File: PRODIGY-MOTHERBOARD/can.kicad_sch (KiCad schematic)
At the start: 1 part, among them U12 SN65HVD232

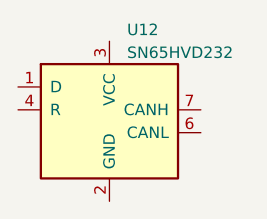
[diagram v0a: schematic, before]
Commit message: project restructure done. Hierarchical sheet done. Outputs/breakouts sheet done
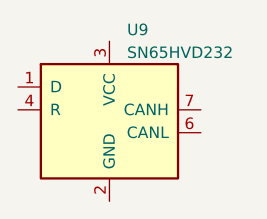
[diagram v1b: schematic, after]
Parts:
- renumbered U12 to U9
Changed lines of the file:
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@@
-(kicad_sch (version 20230121) (generator eeschema)
-  (paper "A4")
-  (symbol (lib_id "Interface_CAN_LIN:SN65HVD232") (at 138.43 93.98 0) (unit 1)
-    (in_bom yes) (on_board yes) (dnp no) (fields_autoplaced)
-    (property "Reference" "U12" (at 140.3859 85.09 0)
-      (effects (font (size 1.27 1.27)) (justify left))
-    )
-    (property "Value" "SN65HVD232" (at 140.3859 87.63 0)
-      (effects (font (size 1.27 1.27)) (justify left))
-    )
-    (property "Footprint" "Package_SO:SOIC-8_3.9x4.9mm_P1.27mm" (at 138.43 106.68 0)
-      (effects (font (size 1.27 1.27)) hide)
-    )
-    (property "Datasheet" "http://www.ti.com/lit/ds/symlink/sn65hvd230.pdf" (at 135.89 83.82 0)
-      (effects (font (size 1.27 1.27)) hide)
-    )
-    (pin "1")
-    (pin "2")
-    (pin "3")
-    (pin "4")
-    (pin "5")
-    (pin "6")
-    (pin "7")
-    (pin "8")
-    (instances
-      (project "PRODIGY-MOTHERBOARD"
-        (path "/f1c25860-8989-4190-bd24-2491d23ca7d9/cf0d8bf1-4632-49df-9398-b3de35528304"
-          (reference "U12") (unit 1)
-        )
-      )
-    )
-  )
+(kicad_sch
+	(version 20231120)
+	(generator "eeschema")
+	(generator_version "8.0")
+	(paper "A4")
+	(symbol
+		(lib_id "Interface_CAN_LIN:SN65HVD232")
+		(at 138.43 93.98 0)
+		(unit 1)
+		(exclude_from_sim no)
+		(in_bom yes)
+		(on_board yes)
+		(dnp no)
+		(fields_autoplaced yes)
+		(property "Reference" "U9"
+			(at 140.3859 85.09 0)
+			(effects
+				(font
+					(size 1.27 1.27)
+				)
+				(justify left)
+			)
+		)
+		(property "Value" "SN65HVD232"
+			(at 140.3859 87.63 0)
+			(effects
+				(font
+					(size 1.27 1.27)
+				)
+				(justify left)
+			)
+		)
+		(property "Footprint" "Package_SO:SOIC-8_3.9x4.9mm_P1.27mm"
+			(at 138.43 106.68 0)
+			(effects
+				(font
+					(size 1.27 1.27)
+				)
+				(hide yes)
+			)
+		)
+		(property "Datasheet" "http://www.ti.com/lit/ds/symlink/sn65hvd230.pdf"
+			(at 135.89 83.82 0)
+			(effects
+				(font
+					(size 1.27 1.27)
+				)
+				(hide yes)
+			)
+		)
+		(property "Description" ""
+			(at 138.43 93.98 0)
+			(effects
+				(font
+					(size 1.27 1.27)
+				)
+				(hide yes)
+			)
+		)
+		(pin "1"
+		)
+		(pin "2"
+		)
+		(pin "3"
+		)
+		(pin "4"
+		)
+		(pin "5"
+		)
+		(pin "6"
+		)
+		(pin "7"
+		)
+		(pin "8"
+		)
+		(instances
+			(project "PRODIGY-MOTHERBOARD"
+				(path "/f1c25860-8989-4190-bd24-2491d23ca7d9/cf0d8bf1-4632-49df-9398-b3de35528304"
+					(reference "U9")
+					(unit 1)
+				)
+			)
+		)
+	)
 )

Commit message: CAN schematic done
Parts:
- removed U9: SN65HVD232, Package_SO:SOIC-8_3.9x4.9mm_P1.27mm, symbol Interface_CAN_LIN:SN65HVD232
- added C58: 100nF, Capacitor_SMD:C_0603_1608Metric, symbol Device:C
- added C59, C60, C61, C62: 100pF, symbol Device:C
- added C63: 4n7, symbol Device:C
- added D29, D30: SD05_SOD323, Diode_SMD:D_SOD-323, symbol Diode:SD05_SOD323
- added L3: L_Iron_Coupled_1324, Inductor_SMD:L_CommonModeChoke_TDK_ACM7060, symbol Device:L_Iron_Coupled_1324
- added R67, R68: 59, Resistor_SMD:R_1206_3216Metric, symbol Device:R
- added U25: TJA1051T-E, Package_SO:SOIC-8_3.9x4.9mm_P1.27mm, symbol Interface_CAN_LIN:TJA1051T-E
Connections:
- new net: C60.1, L3.4, U25.6 (CANL)
- new net: C63.1, R67.2, R68.1
- new net: C59.1, L3.3, U25.7 (CANH)
- new net +3.3V: C58.1, U25.3 (VCC)
- new net CAN_EN: U25.5 (EN)
- new net CAN_H: C61.1, D29.2 (A2), L3.1, R67.1
- new net CAN_L: C62.1, D30.2 (A2), L3.2, R68.2
- new net CAN_RX: U25.4 (RXD)
- new net CAN_SILENT: U25.8 (S)
- new net CAN_TX: U25.1 (TXD)
- new net GND: C58.2, C59.2, C60.2, C61.2, C62.2, C63.2, D29.1 (A1), D30.1 (A1), U25.2 (GND)

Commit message: SPI NFC schematic done.
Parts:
- renumbered C58 to C38, C59 to C39, C60 to C40, C61 to C41, C62 to C42, C63 to C43, D29 to D7, D30 to D8, R67 to R24, R68 to R25, U25 to U10
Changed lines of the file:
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@@
 		(dnp no)
 		(fields_autoplaced yes)
-		(property "Reference" "#PWR0157"
+		(property "Reference" "#PWR057"
 			(at 168.91 109.22 0)
 			(effects
@@
 			(project "PRODIGY-MOTHERBOARD"
 				(path "/f1c25860-8989-4190-bd24-2491d23ca7d9/cf0d8bf1-4632-49df-9398-b3de35528304"
-					(reference "#PWR0157")
+					(reference "#PWR057")
 					(unit 1)
 				)
@@
 		(dnp no)
 		(fields_autoplaced yes)
-		(property "Reference" "C60"
+		(property "Reference" "C40"
 			(at 109.22 100.3299 0)
 			(effects
@@
 			(project "PRODIGY-MOTHERBOARD"
 				(path "/f1c25860-8989-4190-bd24-2491d23ca7d9/cf0d8bf1-4632-49df-9398-b3de35528304"
-					(reference "C60")
+					(reference "C40")
 					(unit 1)
 				)
@@
 		(dnp no)
 		(fields_autoplaced yes)
-		(property "Reference" "#PWR0156"
+		(property "Reference" "#PWR056"
 			(at 137.16 113.03 0)
 			(effects
@@
 			(project "PRODIGY-MOTHERBOARD"
 				(path "/f1c25860-8989-4190-bd24-2491d23ca7d9/cf0d8bf1-4632-49df-9398-b3de35528304"
-					(reference "#PWR0156")
+					(reference "#PWR056")
 					(unit 1)
 				)
@@
 		(dnp no)
 		(fields_autoplaced yes)
-		(property "Reference" "R68"
+		(property "Reference" "R25"
 			(at 161.29 96.5199 0)
 			(effects
@@
 			(project "PRODIGY-MOTHERBOARD"
 				(path "/f1c25860-8989-4190-bd24-2491d23ca7d9/cf0d8bf1-4632-49df-9398-b3de35528304"
-					(reference "R68")
+					(reference "R25")
 					(unit 1)
 				)
@@
 		(dnp no)
 		(fields_autoplaced yes)
-		(property "Reference" "#PWR0154"
+		(property "Reference" "#PWR054"
 			(at 105.41 113.03 0)
 			(effects
@@
 			(project "PRODIGY-MOTHERBOARD"
 				(path "/f1c25860-8989-4190-bd24-2491d23ca7d9/cf0d8bf1-4632-49df-9398-b3de35528304"
-					(reference "#PWR0154")
+					(reference "#PWR054")
 					(unit 1)
 				)
@@
 		(dnp no)
 		(fields_autoplaced yes)
-		(property "Reference" "C63"
+		(property "Reference" "C43"
 			(at 172.72 95.2499 0)
 			(effects
@@
 			(project "PRODIGY-MOTHERBOARD"
 				(path "/f1c25860-8989-4190-bd24-2491d23ca7d9/cf0d8bf1-4632-49df-9398-b3de35528304"
-					(reference "C63")
+					(reference "C43")
 					(unit 1)
 				)
@@
 		(dnp no)
 		(fields_autoplaced yes)
-		(property "Reference" "#PWR0158"
+		(property "Reference" "#PWR058"
 			(at 194.31 119.38 0)
 			(effects
@@
 			(project "PRODIGY-MOTHERBOARD"
 				(path "/f1c25860-8989-4190-bd24-2491d23ca7d9/cf0d8bf1-4632-49df-9398-b3de35528304"
-					(reference "#PWR0158")
+					(reference "#PWR058")
 					(unit 1)
 				)
@@
 		(dnp no)
 		(fields_autoplaced yes)
-		(property "Reference" "D29"
+		(property "Reference" "D7"
 			(at 191.77 105.4099 90)
 			(effects
@@
 			(project "PRODIGY-MOTHERBOARD"
 				(path "/f1c25860-8989-4190-bd24-2491d23ca7d9/cf0d8bf1-4632-49df-9398-b3de35528304"
-					(reference "D29")
+					(reference "D7")
 					(unit 1)
 				)
@@
 		(dnp no)
 		(fields_autoplaced yes)
-		(property "Reference" "#PWR0155"
+		(property "Reference" "#PWR055"
 			(at 123.19 113.03 0)
 			(effects
@@
 			(project "PRODIGY-MOTHERBOARD"
 				(path "/f1c25860-8989-4190-bd24-2491d23ca7d9/cf0d8bf1-4632-49df-9398-b3de35528304"
-					(reference "#PWR0155")
+					(reference "#PWR055")
 					(unit 1)
 				)
@@
 		(dnp no)
 		(fields_autoplaced yes)
-		(property "Reference" "C59"
+		(property "Reference" "C39"
 			(at 95.25 100.3299 0)
 			(effects
@@
 			(project "PRODIGY-MOTHERBOARD"
 				(path "/f1c25860-8989-4190-bd24-2491d23ca7d9/cf0d8bf1-4632-49df-9398-b3de35528304"
-					(reference "C59")
+					(reference "C39")
 					(unit 1)
 				)
@@
 		(dnp no)
 		(fields_autoplaced yes)
-		(property "Reference" "#PWR0153"
+		(property "Reference" "#PWR053"
 			(at 91.44 113.03 0)
 			(effects
@@
 			(project "PRODIGY-MOTHERBOARD"
 				(path "/f1c25860-8989-4190-bd24-2491d23ca7d9/cf0d8bf1-4632-49df-9398-b3de35528304"
-					(reference "#PWR0153")
+					(reference "#PWR053")
 					(unit 1)
 				)
@@
 		(dnp no)
 		(fields_autoplaced yes)
-		(property "Reference" "C62"
+		(property "Reference" "C42"
 			(at 140.97 100.3299 0)
 			(effects
@@
 			(project "PRODIGY-MOTHERBOARD"
 				(path "/f1c25860-8989-4190-bd24-2491d23ca7d9/cf0d8bf1-4632-49df-9398-b3de35528304"
-					(reference "C62")
+					(reference "C42")
 					(unit 1)
 				)
@@
 		(dnp no)
 		(fields_autoplaced yes)
-		(property "Reference" "C61"
+		(property "Reference" "C41"
 			(at 127 100.3299 0)
 			(effects
@@
 			(project "PRODIGY-MOTHERBOARD"
 				(path "/f1c25860-8989-4190-bd24-2491d23ca7d9/cf0d8bf1-4632-49df-9398-b3de35528304"
-					(reference "C61")
+					(reference "C41")
 					(unit 1)
 				)
@@
 		(dnp no)
 		(fields_autoplaced yes)
-		(property "Reference" "C58"
+		(property "Reference" "C38"
 			(at 64.77 72.3899 0)
 			(effects
@@
 			(project "PRODIGY-MOTHERBOARD"
 				(path "/f1c25860-8989-4190-bd24-2491d23ca7d9/cf0d8bf1-4632-49df-9398-b3de35528304"
-					(reference "C58")
+					(reference "C38")
 					(unit 1)
 				)
@@
 		(dnp no)
 		(fields_autoplaced yes)
-		(property "Reference" "U25"
+		(property "Reference" "U10"
 			(at 78.3941 80.01 0)
 			(effects
@@
 			(project "PRODIGY-MOTHERBOARD"
 				(path "/f1c25860-8989-4190-bd24-2491d23ca7d9/cf0d8bf1-4632-49df-9398-b3de35528304"
-					(reference "U25")
+					(reference "U10")
 					(unit 1)
 				)
@@
 		(dnp no)
 		(fields_autoplaced yes)
-		(property "Reference" "#PWR0151"
+		(property "Reference" "#PWR050"
 			(at 60.96 83.82 0)
 			(effects
@@
 			(project "PRODIGY-MOTHERBOARD"
 				(path "/f1c25860-8989-4190-bd24-2491d23ca7d9/cf0d8bf1-4632-49df-9398-b3de35528304"
-					(reference "#PWR0151")
+					(reference "#PWR050")
 					(unit 1)
 				)
@@
 		(dnp no)
 		(fields_autoplaced yes)
-		(property "Reference" "#PWR0152"
+		(property "Reference" "#PWR052"
 			(at 76.2 113.03 0)
 			(effects
@@
 			(project "PRODIGY-MOTHERBOARD"
 				(path "/f1c25860-8989-4190-bd24-2491d23ca7d9/cf0d8bf1-4632-49df-9398-b3de35528304"
-					(reference "#PWR0152")
+					(reference "#PWR052")
 					(unit 1)
 				)
@@
 		(dnp no)
 		(fields_autoplaced yes)
-		(property "Reference" "R67"
+		(property "Reference" "R24"
 			(at 161.29 86.3599 0)
 			(effects
@@
 			(project "PRODIGY-MOTHERBOARD"
 				(path "/f1c25860-8989-4190-bd24-2491d23ca7d9/cf0d8bf1-4632-49df-9398-b3de35528304"
-					(reference "R67")
+					(reference "R24")
 					(unit 1)
 				)
@@
 		(on_board yes)
 		(dnp no)
-		(property "Reference" "D30"
+		(property "Reference" "D8"
 			(at 201.93 105.4099 90)
 			(effects
@@
 			(project "PRODIGY-MOTHERBOARD"
 				(path "/f1c25860-8989-4190-bd24-2491d23ca7d9/cf0d8bf1-4632-49df-9398-b3de35528304"
-					(reference "D30")
+					(reference "D8")
 					(unit 1)
 				)
@@
 		(dnp no)
 		(fields_autoplaced yes)
-		(property "Reference" "#PWR0150"
+		(property "Reference" "#PWR051"
 			(at 76.2 72.39 0)
 			(effects
@@
 			(project "PRODIGY-MOTHERBOARD"
 				(path "/f1c25860-8989-4190-bd24-2491d23ca7d9/cf0d8bf1-4632-49df-9398-b3de35528304"
-					(reference "#PWR0150")
-					(unit 1)
-				)
+					(reference "#PWR051")
+					(unit 1)
+				)

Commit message: Analog schematic finished, except the joystick part.
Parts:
- removed D7, D8: SD05_SOD323, Diode_SMD:D_SOD-323, symbol Diode:SD05_SOD323

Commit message: Added pins to MCU. Added Decoder for SPI SS-Multiplexing.
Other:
- moved on the sheet: C38, C39, C40, C41, C42, C43, L3, R24, R25, U10

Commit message: Added proper debounce filter elements to buttons.
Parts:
- renumbered C38 to C49, C43 to C50, C39 to C51, C40 to C52, C41 to C53, C42 to C54, L3 to L5, R24 to R28, R25 to R29, U10 to U11
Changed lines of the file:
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@@
 		(dnp no)
 		(fields_autoplaced yes)
-		(property "Reference" "#PWR057"
+		(property "Reference" "#PWR064"
 			(at 203.2 105.41 0)
 			(effects
@@
 			(project "PRODIGY-MOTHERBOARD"
 				(path "/f1c25860-8989-4190-bd24-2491d23ca7d9/cf0d8bf1-4632-49df-9398-b3de35528304"
-					(reference "#PWR057")
+					(reference "#PWR064")
 					(unit 1)
 				)
@@
 		(dnp no)
 		(fields_autoplaced yes)
-		(property "Reference" "C40"
+		(property "Reference" "C52"
 			(at 143.51 96.5199 0)
 			(effects
@@
 			(project "PRODIGY-MOTHERBOARD"
 				(path "/f1c25860-8989-4190-bd24-2491d23ca7d9/cf0d8bf1-4632-49df-9398-b3de35528304"
-					(reference "C40")
+					(reference "C52")
 					(unit 1)
 				)
@@
 		(dnp no)
 		(fields_autoplaced yes)
-		(property "Reference" "#PWR056"
+		(property "Reference" "#PWR069"
 			(at 171.45 109.22 0)
 			(effects
@@
 			(project "PRODIGY-MOTHERBOARD"
 				(path "/f1c25860-8989-4190-bd24-2491d23ca7d9/cf0d8bf1-4632-49df-9398-b3de35528304"
-					(reference "#PWR056")
+					(reference "#PWR069")
 					(unit 1)
 				)
@@
 		(dnp no)
 		(fields_autoplaced yes)
-		(property "Reference" "R25"
+		(property "Reference" "R29"
 			(at 195.58 92.7099 0)
 			(effects
@@
 			(project "PRODIGY-MOTHERBOARD"
 				(path "/f1c25860-8989-4190-bd24-2491d23ca7d9/cf0d8bf1-4632-49df-9398-b3de35528304"
-					(reference "R25")
+					(reference "R29")
 					(unit 1)
 				)
@@
 		(dnp no)
 		(fields_autoplaced yes)
-		(property "Reference" "#PWR054"
+		(property "Reference" "#PWR067"
 			(at 139.7 109.22 0)
 			(effects
@@
 			(project "PRODIGY-MOTHERBOARD"
 				(path "/f1c25860-8989-4190-bd24-2491d23ca7d9/cf0d8bf1-4632-49df-9398-b3de35528304"
-					(reference "#PWR054")
+					(reference "#PWR067")
 					(unit 1)
 				)
@@
 		(dnp no)
 		(fields_autoplaced yes)
-		(property "Reference" "C43"
+		(property "Reference" "C50"
 			(at 207.01 91.4399 0)
 			(effects
@@
 			(project "PRODIGY-MOTHERBOARD"
 				(path "/f1c25860-8989-4190-bd24-2491d23ca7d9/cf0d8bf1-4632-49df-9398-b3de35528304"
-					(reference "C43")
+					(reference "C50")
 					(unit 1)
 				)
@@
 		(dnp no)
 		(fields_autoplaced yes)
-		(property "Reference" "#PWR055"
+		(property "Reference" "#PWR068"
 			(at 157.48 109.22 0)
 			(effects
@@
 			(project "PRODIGY-MOTHERBOARD"
 				(path "/f1c25860-8989-4190-bd24-2491d23ca7d9/cf0d8bf1-4632-49df-9398-b3de35528304"
-					(reference "#PWR055")
+					(reference "#PWR068")
 					(unit 1)
 				)
@@
 		(dnp no)
 		(fields_autoplaced yes)
-		(property "Reference" "C39"
+		(property "Reference" "C51"
 			(at 129.54 96.5199 0)
 			(effects
@@
 			(project "PRODIGY-MOTHERBOARD"
 				(path "/f1c25860-8989-4190-bd24-2491d23ca7d9/cf0d8bf1-4632-49df-9398-b3de35528304"
-					(reference "C39")
+					(reference "C51")
 					(unit 1)
 				)
@@
 		(dnp no)
 		(fields_autoplaced yes)
-		(property "Reference" "#PWR053"
+		(property "Reference" "#PWR066"
 			(at 125.73 109.22 0)
 			(effects
@@
 			(project "PRODIGY-MOTHERBOARD"
 				(path "/f1c25860-8989-4190-bd24-2491d23ca7d9/cf0d8bf1-4632-49df-9398-b3de35528304"
-					(reference "#PWR053")
+					(reference "#PWR066")
 					(unit 1)
 				)
@@
 		(dnp no)
 		(fields_autoplaced yes)
-		(property "Reference" "C42"
+		(property "Reference" "C54"
 			(at 175.26 96.5199 0)
 			(effects
@@
 			(project "PRODIGY-MOTHERBOARD"
 				(path "/f1c25860-8989-4190-bd24-2491d23ca7d9/cf0d8bf1-4632-49df-9398-b3de35528304"
-					(reference "C42")
+					(reference "C54")
 					(unit 1)
 				)
@@
 		(dnp no)
 		(fields_autoplaced yes)
-		(property "Reference" "C41"
+		(property "Reference" "C53"
 			(at 161.29 96.5199 0)
 			(effects
@@
 			(project "PRODIGY-MOTHERBOARD"
 				(path "/f1c25860-8989-4190-bd24-2491d23ca7d9/cf0d8bf1-4632-49df-9398-b3de35528304"
-					(reference "C41")
+					(reference "C53")
 					(unit 1)
 				)
@@
 		(dnp no)
 		(fields_autoplaced yes)
-		(property "Reference" "C38"
+		(property "Reference" "C49"
 			(at 99.06 68.5799 0)
 			(effects
@@
 			(project "PRODIGY-MOTHERBOARD"
 				(path "/f1c25860-8989-4190-bd24-2491d23ca7d9/cf0d8bf1-4632-49df-9398-b3de35528304"
-					(reference "C38")
+					(reference "C49")
 					(unit 1)
 				)
@@
 		(dnp no)
 		(fields_autoplaced yes)
-		(property "Reference" "U10"
+		(property "Reference" "U11"
 			(at 112.6841 76.2 0)
 			(effects
@@
 			(project "PRODIGY-MOTHERBOARD"
 				(path "/f1c25860-8989-4190-bd24-2491d23ca7d9/cf0d8bf1-4632-49df-9398-b3de35528304"
-					(reference "U10")
+					(reference "U11")
 					(unit 1)
 				)
@@
 		(dnp no)
 		(fields_autoplaced yes)
-		(property "Reference" "L3"
+		(property "Reference" "L5"
 			(at 147.701 81.28 0)
 			(effects
@@
 			(project "PRODIGY-MOTHERBOARD"
 				(path "/f1c25860-8989-4190-bd24-2491d23ca7d9/cf0d8bf1-4632-49df-9398-b3de35528304"
-					(reference "L3")
+					(reference "L5")
 					(unit 1)
 				)
@@
 		(dnp no)
 		(fields_autoplaced yes)
-		(property "Reference" "#PWR050"
+		(property "Reference" "#PWR063"
 			(at 95.25 80.01 0)
 			(effects
@@
 			(project "PRODIGY-MOTHERBOARD"
 				(path "/f1c25860-8989-4190-bd24-2491d23ca7d9/cf0d8bf1-4632-49df-9398-b3de35528304"
-					(reference "#PWR050")
+					(reference "#PWR063")
 					(unit 1)
 				)
@@
 		(dnp no)
 		(fields_autoplaced yes)
-		(property "Reference" "#PWR052"
+		(property "Reference" "#PWR065"
 			(at 110.49 109.22 0)
 			(effects
@@
 			(project "PRODIGY-MOTHERBOARD"
 				(path "/f1c25860-8989-4190-bd24-2491d23ca7d9/cf0d8bf1-4632-49df-9398-b3de35528304"
-					(reference "#PWR052")
+					(reference "#PWR065")
 					(unit 1)
 				)
@@
 		(dnp no)
 		(fields_autoplaced yes)
-		(property "Reference" "R24"
+		(property "Reference" "R28"
 			(at 195.58 82.5499 0)
 			(effects
@@
 			(project "PRODIGY-MOTHERBOARD"
 				(path "/f1c25860-8989-4190-bd24-2491d23ca7d9/cf0d8bf1-4632-49df-9398-b3de35528304"
-					(reference "R24")
+					(reference "R28")
 					(unit 1)
 				)
@@
 		(dnp no)
 		(fields_autoplaced yes)
-		(property "Reference" "#PWR051"
+		(property "Reference" "#PWR062"
 			(at 110.49 68.58 0)
 			(effects
@@
 			(project "PRODIGY-MOTHERBOARD"
 				(path "/f1c25860-8989-4190-bd24-2491d23ca7d9/cf0d8bf1-4632-49df-9398-b3de35528304"
-					(reference "#PWR051")
-					(unit 1)
-				)
+					(reference "#PWR062")
+					(unit 1)
+				)

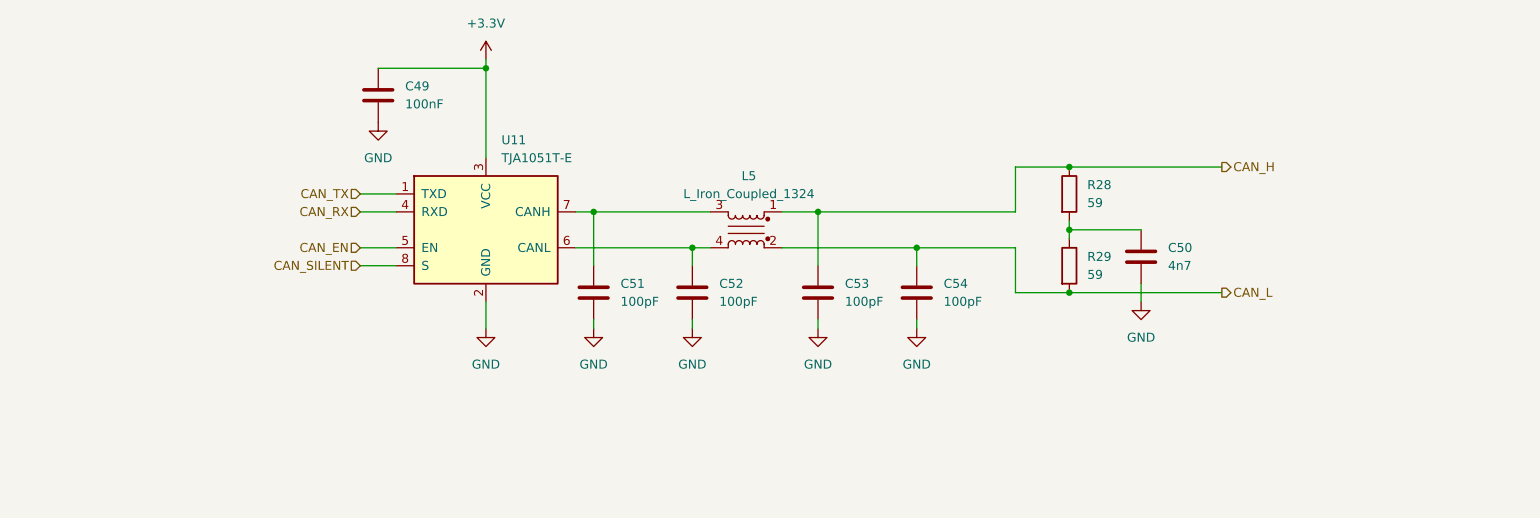
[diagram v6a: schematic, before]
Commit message: Submitted V0 for evaluation. Avaiting feedback.
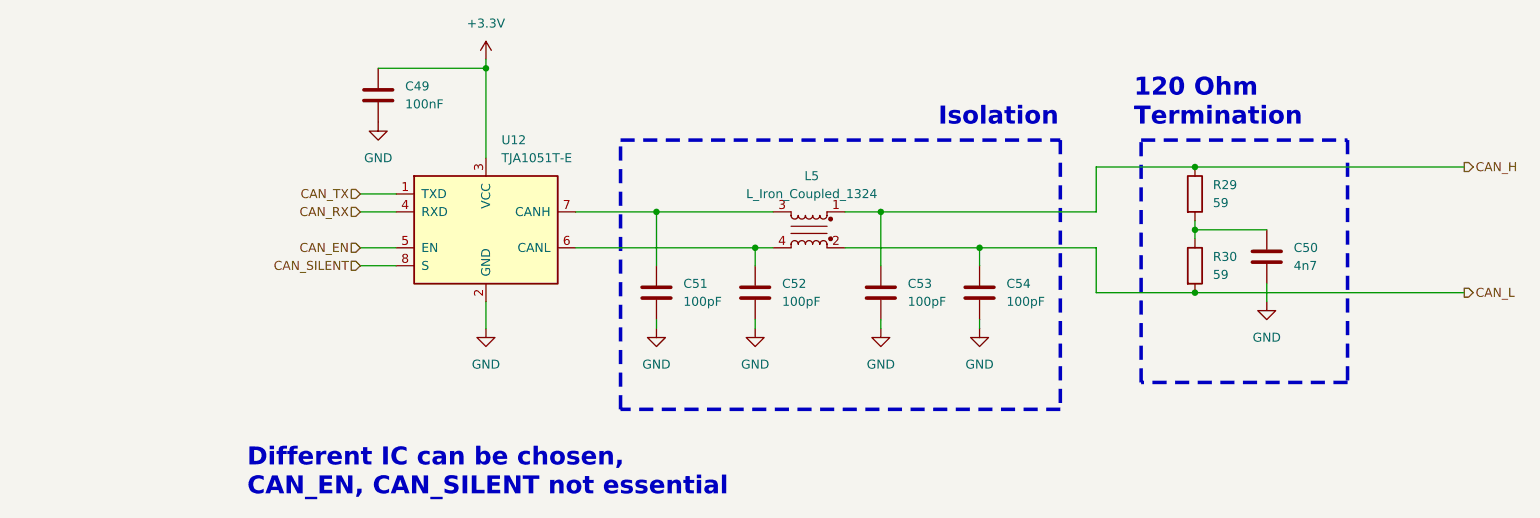
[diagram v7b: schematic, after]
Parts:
- renumbered R28 to R29, R29 to R30, U11 to U12
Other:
- note added: "120 Ohm Termination"
- note added: "Different IC can be chosen, CAN_EN, CAN_SILENT not essential"
- note added: "Isolation"
- moved on the sheet: C50, C51, C52, C53, C54, L5, R29, R30
